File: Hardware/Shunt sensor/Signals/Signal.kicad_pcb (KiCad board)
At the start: 2 copper layers, 55.4 x 29.5 mm, 22 parts, among them Q1 Q_NPN_Darlington_BEC, U1 Signals_MCC, U2 LM324, U3 INA826_D_8

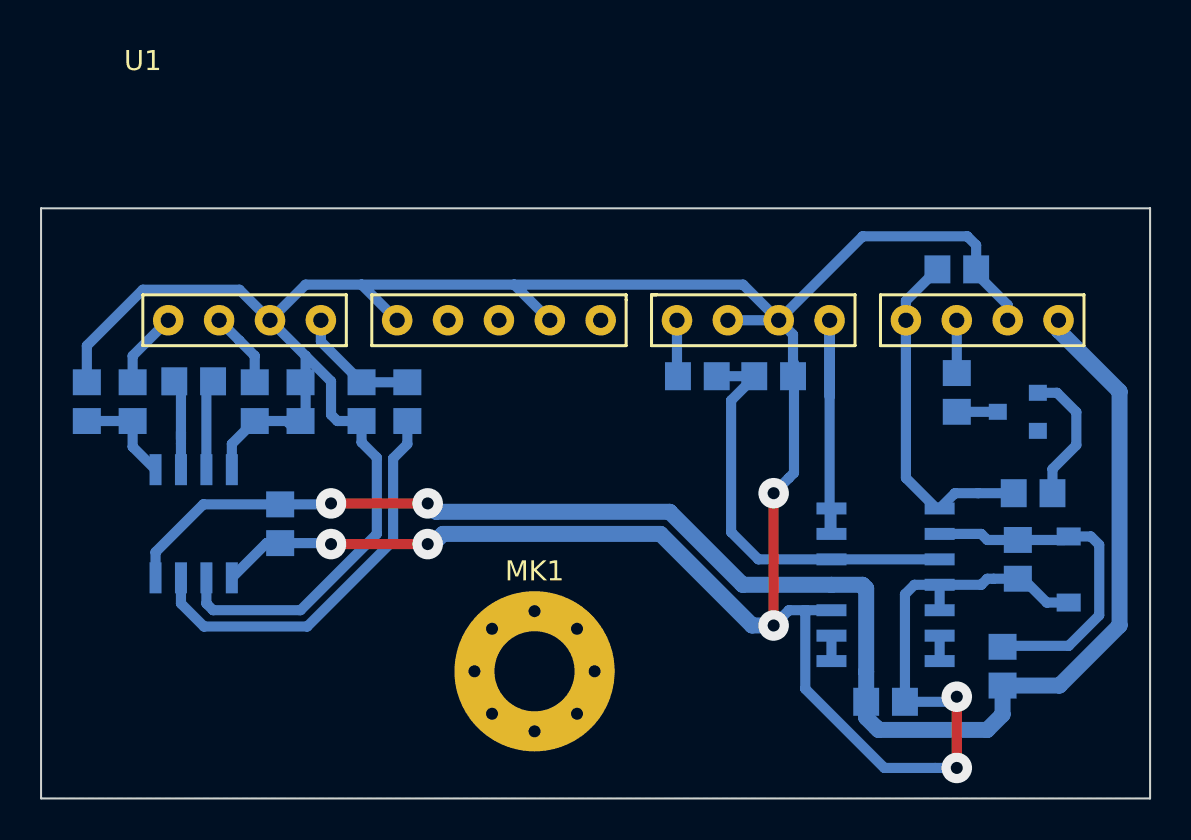
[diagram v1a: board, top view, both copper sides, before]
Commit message: shunt signals updated
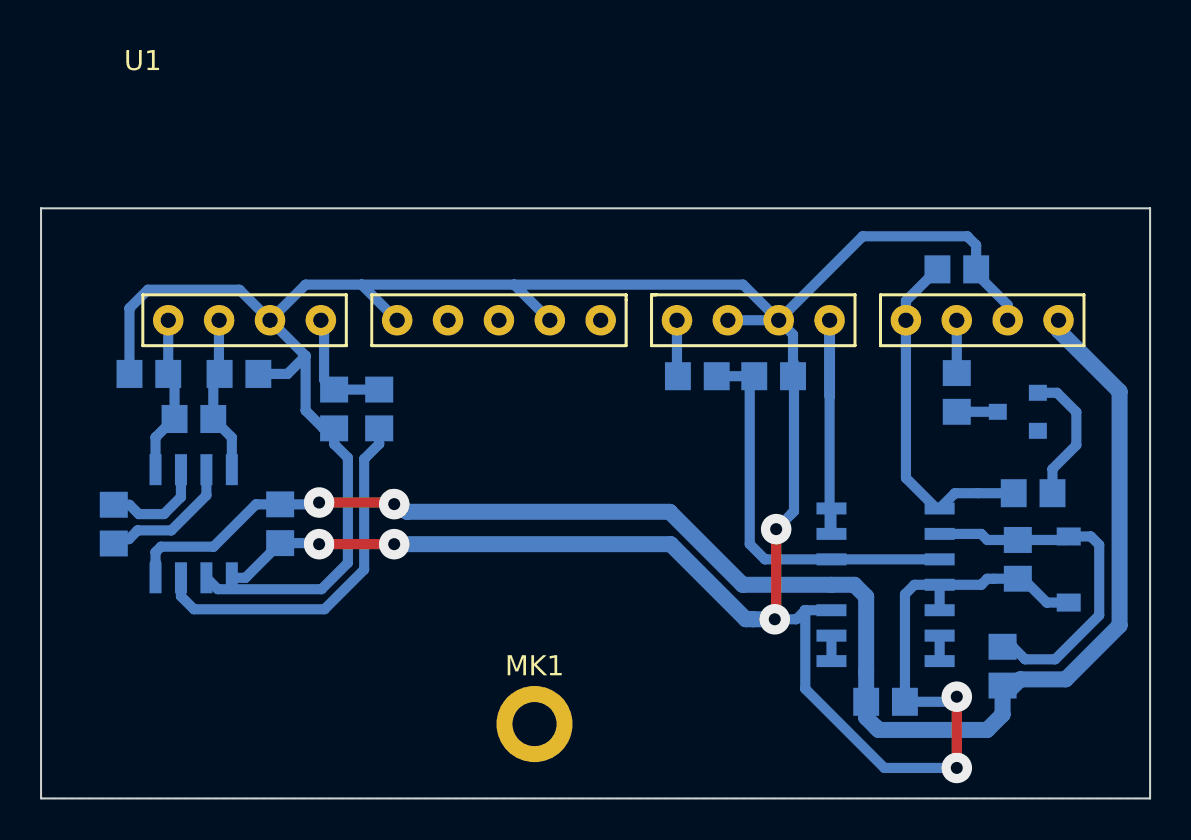
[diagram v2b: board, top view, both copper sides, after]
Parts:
- removed R7, R8: ??, Resistor_SMD:R_0805_2012Metric_Pad1.29x1.40mm_HandSolder
- added R11: ??, Resistor_SMD:R_0805_2012Metric_Pad1.29x1.40mm_HandSolder, B.Cu at (31.0, 25.2)
- MK1: footprint MountingHole:MountingHole_4mm_Pad_Via -> MountingHole:MountingHole_2.2mm_M2_DIN965_Pad
- moved R6 8.17 mm to (27.0, 30.5), turned to 90 degrees
- moved R9 3.39 mm to (28.8, 23.0), turned to 180 degrees
- moved R10 3.37 mm to (33.2, 23.0), turned to 180 degrees
- moved MK1 2.64 mm to (48.0, 40.5)
- moved R5 1.45 mm to (40.2, 24.8)
- moved C4 1.42 mm to (38.0, 24.8)
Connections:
- R10 pad 2: Net-(R10-Pad2) -> /Vpanel_SIG
- R9 pad 1: GNDA -> /Vpanel_Ref
- R9 pad 2: Net-(R7-Pad1) -> GNDA
- U2 pad 4: Net-(U2-Pad4) -> +5VA
- U3 pad 1: Net-(R7-Pad1) -> /Vpanel_Ref
- U3 pad 4: Net-(R10-Pad2) -> /Vpanel_SIG
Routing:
- net +5VA: track 87.2 -> 80.9 mm
- net GNDA: track 177.8 -> 172.3 mm
- net Net-(R7-Pad1): track 5.19 -> 0.00 mm
- net Net-(R10-Pad2): track 4.99 -> 0.00 mm
- net /Vpanel_Ref: track 3.83 -> 8.45 mm
- net /Vpanel_SIG: track 3.83 -> 8.37 mm
- net Net-(R6-Pad1): track 4.55 -> 6.90 mm
- net Net-(R5-Pad2): track 20.4 -> 18.5 mm
- net Net-(R33-Pad1): track 21.1 -> 20.2 mm
- net /+3.9V: track 17.5 -> 18.0 mm
